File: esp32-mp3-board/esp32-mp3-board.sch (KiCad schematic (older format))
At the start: 39 parts, among them J1 USB_C_Receptacle_USB2.0, J2 Conn_01x02, J3 UART, J4 TOUCH, J5 Conn_01x04, Q1 S9013, Q2 S9013, SW1 SW_PUSH, U1 AP2112K-3.3, U2 ESP32-WROOM-32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

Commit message: update
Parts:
- added R10, R11: 5.1K, OPL_Resistor:R0603, symbol Device:R_Small
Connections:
- wire segments 134 -> 140
- no-connect marks 30 -> 28
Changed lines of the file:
@@
 NoConn ~ 1600 3450
 NoConn ~ 1600 3550
-NoConn ~ 1600 2650
-NoConn ~ 1600 2550
 $Comp
 L power:GND #PWR02
@@
 Wire Wire Line
 	8800 900  8850 900
+$Comp
+L Device:R_Small R10
+U 1 1 5ED8357F
+P 1800 2550
+F 0 "R10" H 1859 2596 50  0000 L CNN
+F 1 "5.1K" H 1859 2505 50  0000 L CNN
+F 2 "OPL_Resistor:R0603" H 1800 2550 50  0001 C CNN
+F 3 "~" H 1800 2550 50  0001 C CNN
+	1    1800 2550
+	0    1    1    0
+$EndComp
+$Comp
+L Device:R_Small R11
+U 1 1 5ED838E7
+P 1800 2650
+F 0 "R11" H 1859 2696 50  0000 L CNN
+F 1 "5.1K" H 1859 2605 50  0000 L CNN
+F 2 "OPL_Resistor:R0603" H 1800 2650 50  0001 C CNN
+F 3 "~" H 1800 2650 50  0001 C CNN
+	1    1800 2650
+	0    1    1    0
+$EndComp
+Wire Wire Line
+	1600 2550 1700 2550
+Wire Wire Line
+	1600 2650 1700 2650
+Wire Wire Line
+	1900 2550 1950 2550
+Wire Wire Line
+	1950 2550 1950 2650
+Wire Wire Line
+	1950 2650 1900 2650
+$Comp
+L power:GND #PWR04
+U 1 1 5ED937DF
+P 1950 2750
+F 0 "#PWR04" H 1950 2500 50  0001 C CNN
+F 1 "GND" H 1955 2577 50  0000 C CNN
+F 2 "" H 1950 2750 50  0001 C CNN
+F 3 "" H 1950 2750 50  0001 C CNN
+	1    1950 2750
+	1    0    0    -1
+$EndComp
+Wire Wire Line
+	1950 2650 1950 2750
+Connection ~ 1950 2650
 $EndSCHEMATC

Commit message: WS2812S まわり修正
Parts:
- removed R8: 100, OPL_Resistor:R0603, symbol Device:R_Small
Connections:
- wire segments 140 -> 139
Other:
- moved on the sheet: D3, R7
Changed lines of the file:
@@
 L LED:WS2812S D3
 U 1 1 5EC85112
-P 9150 1250
-F 0 "D3" H 9494 1296 50  0000 L CNN
-F 1 "WS2812S" H 9494 1205 50  0000 L CNN
-F 2 "LED_SMD:LED_WS2812_PLCC6_5.0x5.0mm_P1.6mm" H 9200 950 50  0001 L TNN
-F 3 "http://www.world-semi.com/DownLoadFile/115" H 9250 875 50  0001 L TNN
-	1    9150 1250
+P 9350 1250
+F 0 "D3" H 9694 1296 50  0000 L CNN
+F 1 "WS2812S" H 9694 1205 50  0000 L CNN
+F 2 "LED_SMD:LED_WS2812_PLCC6_5.0x5.0mm_P1.6mm" H 9400 950 50  0001 L TNN
+F 3 "http://www.world-semi.com/DownLoadFile/115" H 9450 875 50  0001 L TNN
+	1    9350 1250
 	1    0    0    -1
 $EndComp
@@
 L Device:R_Small R7
 U 1 1 5EC86C0E
-P 8700 1250
-F 0 "R7" V 8504 1250 50  0000 C CNN
-F 1 "100" V 8595 1250 50  0000 C CNN
-F 2 "OPL_Resistor:R0603" H 8700 1250 50  0001 C CNN
-F 3 "~" H 8700 1250 50  0001 C CNN
-	1    8700 1250
+P 8900 1250
+F 0 "R7" V 8704 1250 50  0000 C CNN
+F 1 "100" V 8795 1250 50  0000 C CNN
+F 2 "OPL_Resistor:R0603" H 8900 1250 50  0001 C CNN
+F 3 "~" H 8900 1250 50  0001 C CNN
+	1    8900 1250
 	0    1    1    0
 $EndComp
-Text Label 8500 1250 0    50   ~ 0
+Text Label 8700 1250 0    50   ~ 0
 IO4
 $Comp
 L power:GND #PWR029
 U 1 1 5EC9218B
-P 9150 1650
-F 0 "#PWR029" H 9150 1400 50  0001 C CNN
-F 1 "GND" H 9155 1477 50  0000 C CNN
-F 2 "" H 9150 1650 50  0001 C CNN
-F 3 "" H 9150 1650 50  0001 C CNN
-	1    9150 1650
-	1    0    0    -1
-$EndComp
-Wire Wire Line
-	8800 1250 8850 1250
-Wire Wire Line
-	8500 1250 8600 1250
+P 9350 1650
+F 0 "#PWR029" H 9350 1400 50  0001 C CNN
+F 1 "GND" H 9355 1477 50  0000 C CNN
+F 2 "" H 9350 1650 50  0001 C CNN
+F 3 "" H 9350 1650 50  0001 C CNN
+	1    9350 1650
+	1    0    0    -1
+$EndComp
+Wire Wire Line
+	9000 1250 9050 1250
+Wire Wire Line
+	8700 1250 8800 1250
 Text Label 7100 3100 0    50   ~ 0
 IO4
@@
 $EndComp
 $Comp
-L Device:R_Small R8
-U 1 1 5ECC4561
-P 9650 1250
-F 0 "R8" V 9454 1250 50  0000 C CNN
-F 1 "100" V 9545 1250 50  0000 C CNN
-F 2 "OPL_Resistor:R0603" H 9650 1250 50  0001 C CNN
-F 3 "~" H 9650 1250 50  0001 C CNN
-	1    9650 1250
-	0    1    1    0
-$EndComp
-Text Label 9450 1250 0    50   ~ 0
-IO4
-$Comp
 L power:GND #PWR031
 U 1 1 5ECC4576
@@
 	1    0    0    -1
 $EndComp
-Wire Wire Line
-	9750 1250 9800 1250
-Wire Wire Line
-	9450 1250 9550 1250
 NoConn ~ 10400 1250
 Wire Notes Line
@@
 L power:+3V3 #PWR0103
 U 1 1 5EF0818A
-P 9150 900
-F 0 "#PWR0103" H 9150 750 50  0001 C CNN
-F 1 "+3V3" H 9165 1073 50  0000 C CNN
-F 2 "" H 9150 900 50  0001 C CNN
-F 3 "" H 9150 900 50  0001 C CNN
-	1    9150 900
+P 9350 900
+F 0 "#PWR0103" H 9350 750 50  0001 C CNN
+F 1 "+3V3" H 9365 1073 50  0000 C CNN
+F 2 "" H 9350 900 50  0001 C CNN
+F 3 "" H 9350 900 50  0001 C CNN
+	1    9350 900
 	1    0    0    -1
 $EndComp
@@
 Text Label 10000 900  1    50   ~ 0
 VDD
-Text Label 9050 900  1    50   ~ 0
+Text Label 9250 900  1    50   ~ 0
 VDD
 $Comp
@@
 	10000 900  10000 950
 Wire Wire Line
-	9150 900  9150 950
-Wire Wire Line
-	9050 900  9050 950
+	9350 900  9350 950
+Wire Wire Line
+	9250 900  9250 950
 Wire Wire Line
 	8750 900  8800 900
@@
 	8300 900  8450 900
 Wire Wire Line
-	9150 1550 9150 1650
+	9350 1550 9350 1650
 Wire Wire Line
 	10100 1550 10100 1650
@@
 	1950 2650 1950 2750
 Connection ~ 1950 2650
+Wire Wire Line
+	9650 1250 9800 1250
 $EndSCHEMATC

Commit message: add esp32-mp3-board
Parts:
- D1: footprint OPL_Discrete_Semiconductor:SOD-123 -> Diode_SMD:D_SOD-123
- D2: footprint LED_SMD:LED_0201_0603Metric -> LED_SMD:LED_0603_1608Metric
- D5: symbol OPL_Discrete_Semiconductor:SMD-DIODE-SWITCH-1N4148_LL-34_ -> esp32-mp3-board-rescue:SMD-DIODE-SWITCH-1N4148_LL-34_-OPL_Discrete_Semiconductor
- L1, L2: symbol OPL_Filters_and_Magnetic_Beads:SMD-FERRITE-CHIP-120-OHM-500MA_0603_ -> esp32-mp3-board-rescue:SMD-FERRITE-CHIP-120-OHM-500MA_0603_-OPL_Filters_and_Magnetic_Beads
- Q1, Q2: symbol OPL_Discrete_Semiconductor:SMD-TRANSISTORS-NPN-25V-500MA-S9013_SOT-23_ -> esp32-mp3-board-rescue:SMD-TRANSISTORS-NPN-25V-500MA-S9013_SOT-23_-OPL_Discrete_Semiconductor
- SW1: symbol open-automation:SW_PUSH -> esp32-mp3-board-rescue:SW_PUSH-open-automation
- U3: symbol open-automation:MAX98357AETE+T -> esp32-mp3-board-rescue:MAX98357AETE+T-open-automation
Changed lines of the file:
@@
 $EndComp
 $Comp
-L open-automation:MAX98357AETE+T U3
+L esp32-mp3-board-rescue:MAX98357AETE+T-open-automation U3
 U 1 1 5EB58F98
 P 3250 2650
@@
 $EndComp
 $Comp
-L OPL_Discrete_Semiconductor:SMD-TRANSISTORS-NPN-25V-500MA-S9013_SOT-23_ Q1
+L esp32-mp3-board-rescue:SMD-TRANSISTORS-NPN-25V-500MA-S9013_SOT-23_-OPL_Discrete_Semiconductor Q1
 U 1 1 5EB9E4A7
 P 5250 950
@@
 $EndComp
 $Comp
-L OPL_Discrete_Semiconductor:SMD-TRANSISTORS-NPN-25V-500MA-S9013_SOT-23_ Q2
+L esp32-mp3-board-rescue:SMD-TRANSISTORS-NPN-25V-500MA-S9013_SOT-23_-OPL_Discrete_Semiconductor Q2
 U 1 1 5EB9E721
 P 5250 1450
@@
 F 0 "D2" V 5946 1232 50  0000 R CNN
 F 1 "LED" V 5855 1232 50  0000 R CNN
-F 2 "LED_SMD:LED_0201_0603Metric" V 5900 1300 50  0001 C CNN
+F 2 "LED_SMD:LED_0603_1608Metric" V 5900 1300 50  0001 C CNN
 F 3 "~" V 5900 1300 50  0001 C CNN
 	1    5900 1300
@@
 	3800 2800 3850 2800
 $Comp
-L OPL_Filters_and_Magnetic_Beads:SMD-FERRITE-CHIP-120-OHM-500MA_0603_ L1
+L esp32-mp3-board-rescue:SMD-FERRITE-CHIP-120-OHM-500MA_0603_-OPL_Filters_and_Magnetic_Beads L1
 U 1 1 5EC28B26
 P 4150 2500
@@
 $EndComp
 $Comp
-L OPL_Filters_and_Magnetic_Beads:SMD-FERRITE-CHIP-120-OHM-500MA_0603_ L2
+L esp32-mp3-board-rescue:SMD-FERRITE-CHIP-120-OHM-500MA_0603_-OPL_Filters_and_Magnetic_Beads L2
 U 1 1 5EC2B1B8
 P 4150 2600
@@
 	1650 1900 1650 500
 $Comp
-L open-automation:SW_PUSH SW1
+L esp32-mp3-board-rescue:SW_PUSH-open-automation SW1
 U 1 1 5EE5400E
 P 3950 1300
@@
 F 0 "D1" H 1950 795 50  0000 C CNN
 F 1 "D_Schottky" H 1950 886 50  0000 C CNN
-F 2 "OPL_Discrete_Semiconductor:SOD-123" V 1950 1000 50  0001 C CNN
+F 2 "Diode_SMD:D_SOD-123" V 1950 1000 50  0001 C CNN
 F 3 "~" V 1950 1000 50  0001 C CNN
 	1    1950 1000
@@
 VDD
 $Comp
-L OPL_Discrete_Semiconductor:SMD-DIODE-SWITCH-1N4148_LL-34_ D5
+L esp32-mp3-board-rescue:SMD-DIODE-SWITCH-1N4148_LL-34_-OPL_Discrete_Semiconductor D5
 U 1 1 5EBC2D6D
 P 8600 900

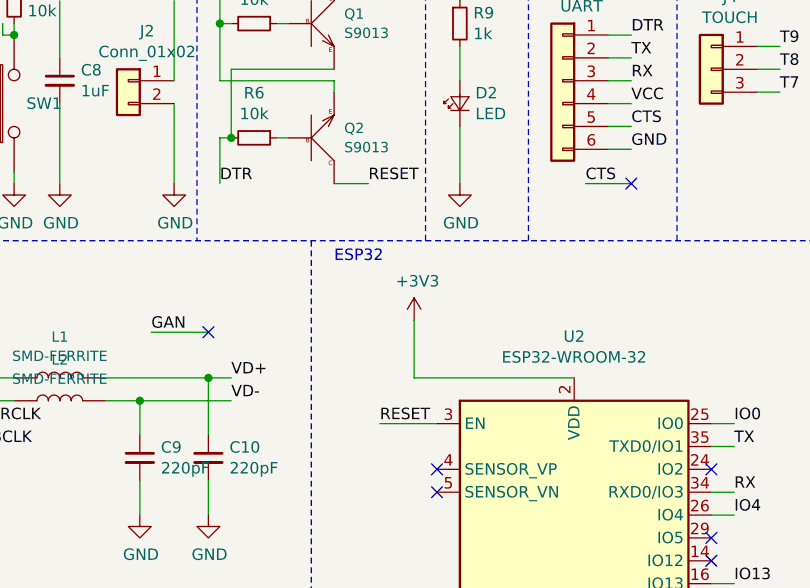
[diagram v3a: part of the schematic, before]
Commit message: RESET回路 EN端子指定の誤りを修正
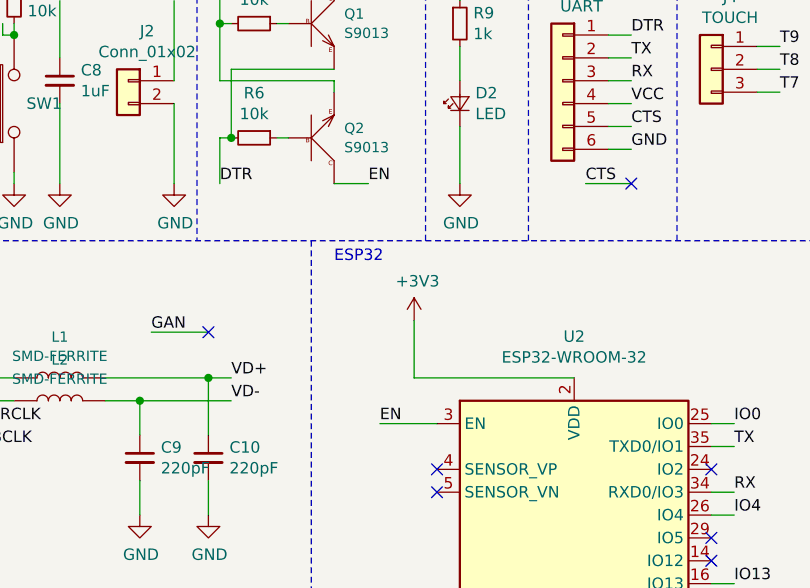
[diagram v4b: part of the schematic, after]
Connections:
- net RESET: no longer Q2.3 (C), U2.3 (EN)
- new net EN: Q2.3 (C), U2.3 (EN)
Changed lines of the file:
@@
 IO0
 Text Label 5500 1650 0    50   ~ 0
-RESET
+EN
 Wire Wire Line
 	5350 750  5450 750
@@
 	7000 3400 7100 3400
 Text Label 5550 2700 0    50   ~ 0
-RESET
+EN
 Wire Wire Line
 	5800 2700 5550 2700

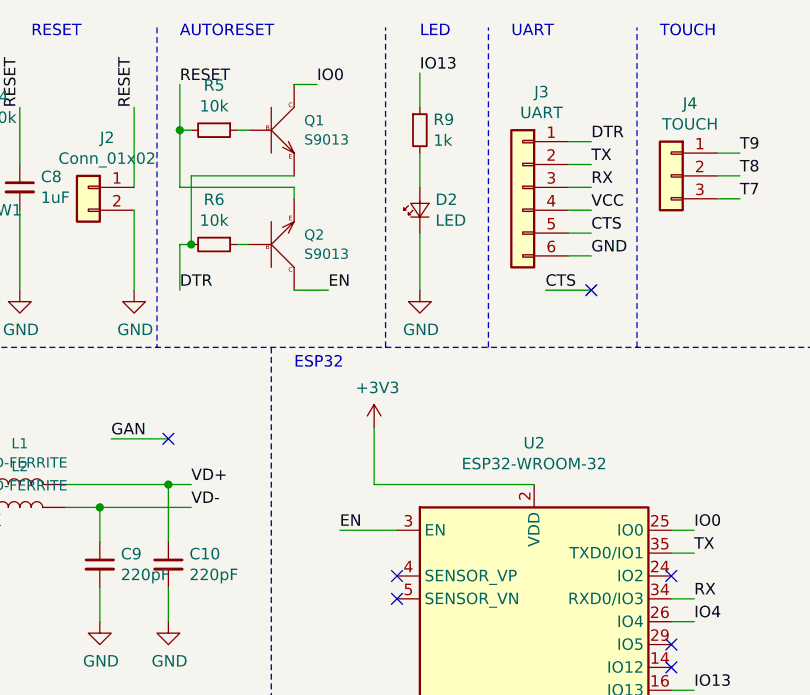
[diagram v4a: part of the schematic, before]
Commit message: RTS追加 CTS回路修正
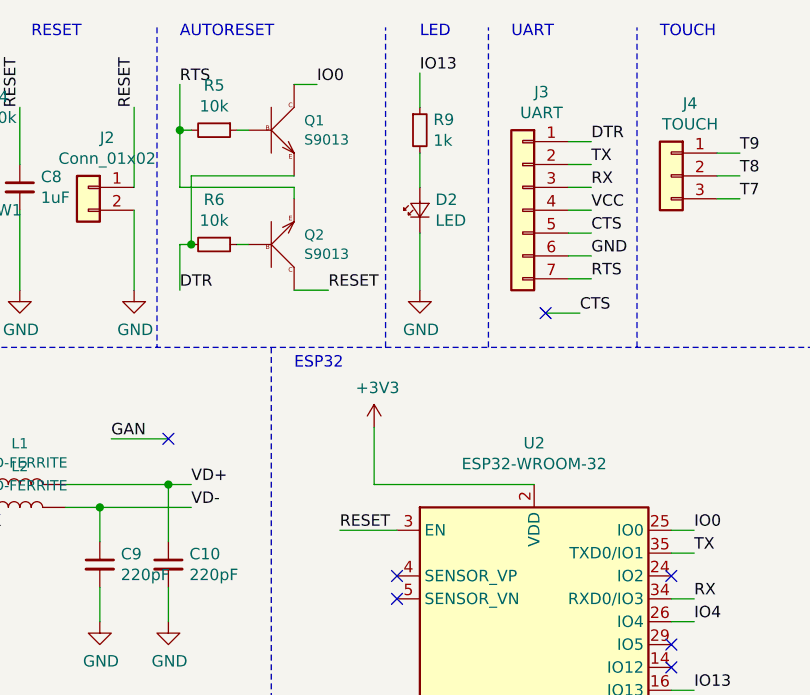
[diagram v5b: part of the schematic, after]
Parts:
- removed J3: UART, OPL_Connector:H6-2.54, symbol Connector_Generic:Conn_01x06
- added J3: UART, symbol Connector_Generic:Conn_01x07
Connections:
- net EN is gone; now on net RESET: Q2.3 (C), U2.3 (EN)
- net +3V3: now also J3.4 (Pin_4)
- net CTS: now also J3.5 (Pin_5)
- net DTR: now also J3.1 (Pin_1)
- net GND: now also J3.6 (Pin_6)
- net RESET: no longer Q2.2 (E), R5.2
- net RX: now also J3.3 (Pin_3)
- net TX: now also J3.2 (Pin_2)
- new net RTS: J3.7 (Pin_7), Q2.2 (E), R5.2
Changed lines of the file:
@@
 $EndComp
 Text Label 4850 750  0    50   ~ 0
-RESET
+RTS
 Text Label 4850 1650 0    50   ~ 0
 DTR
@@
 IO0
 Text Label 5500 1650 0    50   ~ 0
-EN
+RESET
 Wire Wire Line
 	5350 750  5450 750
@@
 Wire Notes Line
 	6200 1900 6200 500
-$Comp
-L Connector_Generic:Conn_01x06 J3
-U 1 1 5EBB3FDB
-P 6350 1200
-F 0 "J3" H 6268 1617 50  0000 C CNN
-F 1 "UART" H 6268 1526 50  0000 C CNN
-F 2 "OPL_Connector:H6-2.54" H 6350 1200 50  0001 C CNN
-F 3 "~" H 6350 1200 50  0001 C CNN
-	1    6350 1200
-	-1   0    0    -1
-$EndComp
 Text Label 6650 1000 0    50   ~ 0
 DTR
@@
 	7000 3400 7100 3400
 Text Label 5550 2700 0    50   ~ 0
-EN
+RESET
 Wire Wire Line
 	5800 2700 5550 2700
@@
 	4550 2300 4800 2300
 NoConn ~ 4800 2300
-Text Label 6450 1650 0    50   ~ 0
-CTS
-NoConn ~ 6650 1650
-Wire Wire Line
-	6650 1650 6450 1650
 Wire Wire Line
 	900  1250 900  1400
@@
 Wire Wire Line
 	9650 1250 9800 1250
+$Comp
+L Connector_Generic:Conn_01x07 J3
+U 1 1 5F7F57FD
+P 6350 1300
+F 0 "J3" H 6268 1817 50  0000 C CNN
+F 1 "UART" H 6268 1726 50  0000 C CNN
+F 2 "" H 6350 1300 50  0001 C CNN
+F 3 "~" H 6350 1300 50  0001 C CNN
+	1    6350 1300
+	-1   0    0    -1
+$EndComp
+Text Label 6650 1600 0    50   ~ 0
+RTS
+Wire Wire Line
+	6550 1600 6650 1600
+Wire Wire Line
+	6450 1750 6600 1750
+Text Label 6600 1750 0    50   ~ 0
+CTS
+NoConn ~ 6450 1750
 $EndSCHEMATC
